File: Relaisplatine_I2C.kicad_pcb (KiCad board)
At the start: 2 copper layers, 85.1 x 114.9 mm, 74 parts, among them J1 K, J1.1 G1-K, J1.1a1001 G1-J, J1.1a1002 G1-K, J1.1a1003 G1-K, J1.1a1004 G1-K, J1.1a1005 G1-K, J1.1a1006 G1-K, J1.1a1007 G1-K, J1.2 G1-J, J1.2a1001 G1-K, J1.2a1002 G1-J, J1.2a1003 G1-J, J1.2a1004 G1-J, J1.2a1005 G1-J, J1.2a1006 G1-J, J1.2a1007 G1-J, J10 I²C, J11 Relais-Power, J12 Int, J2 J, J2.1 G2-K, J2.1a1001 G1-J, J2.2 G2-J, J2.2a1001 G2-K, J3.1 G3-K, J3.2 G3-J, J4.1 G4-K, J4.2 G4-J, J5.1 G5-K, J5.2 G5-J, J6.1 G6-K, J6.2 G6-J, J7.1 G7-K, J7.2 G7-J, J8.1 G8-K, J8.2 G8-J, U1 ULN2803A, U2 PCF8574

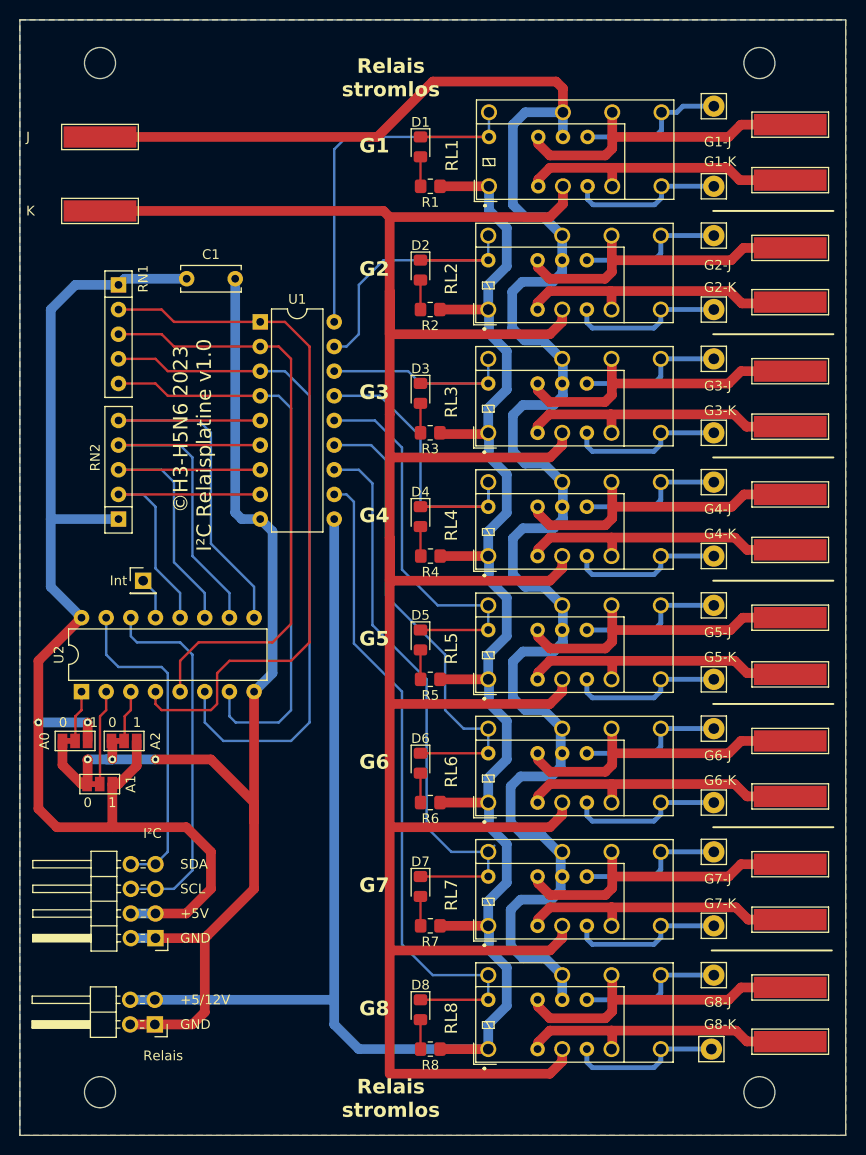
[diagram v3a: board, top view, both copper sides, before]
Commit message: Beschriftung für Gx-J|K vergrößert
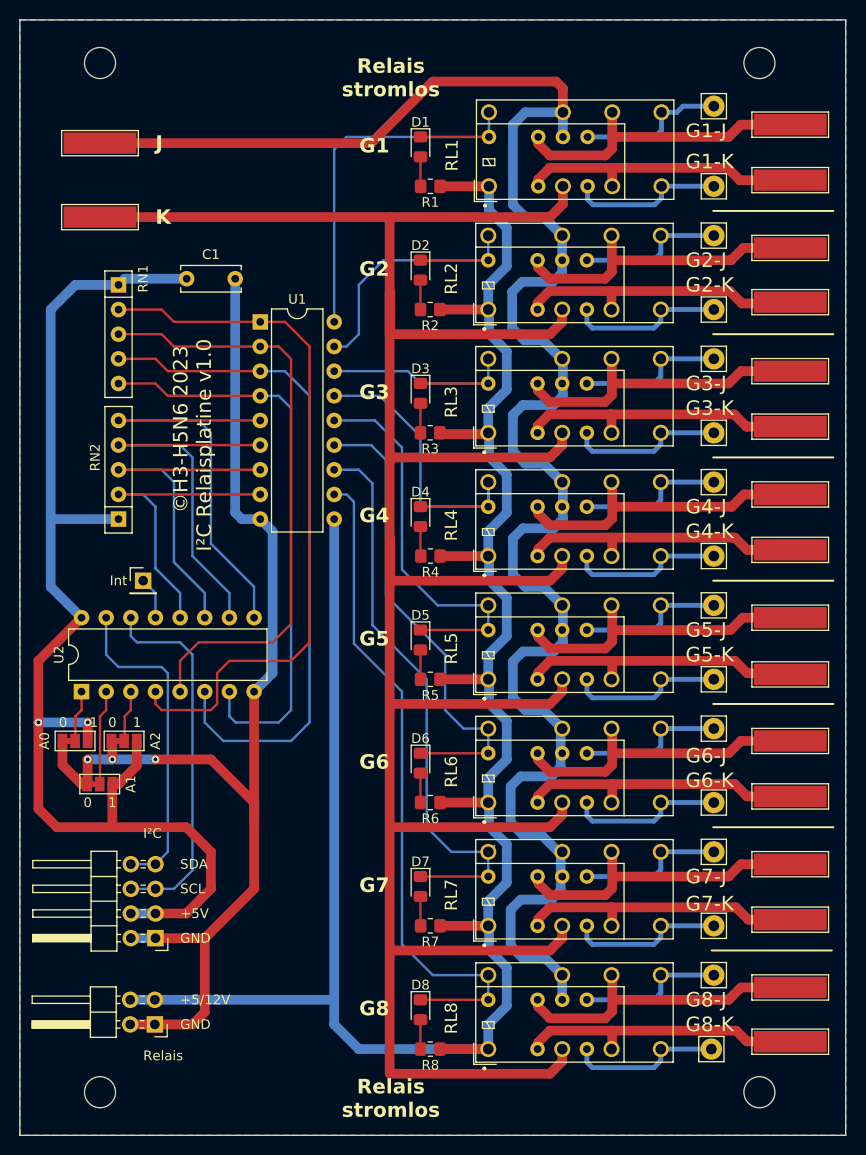
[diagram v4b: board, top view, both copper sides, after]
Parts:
- moved J1 0.64 mm to (67.3, 64.1)
- moved J2 0.63 mm to (67.3, 56.5)

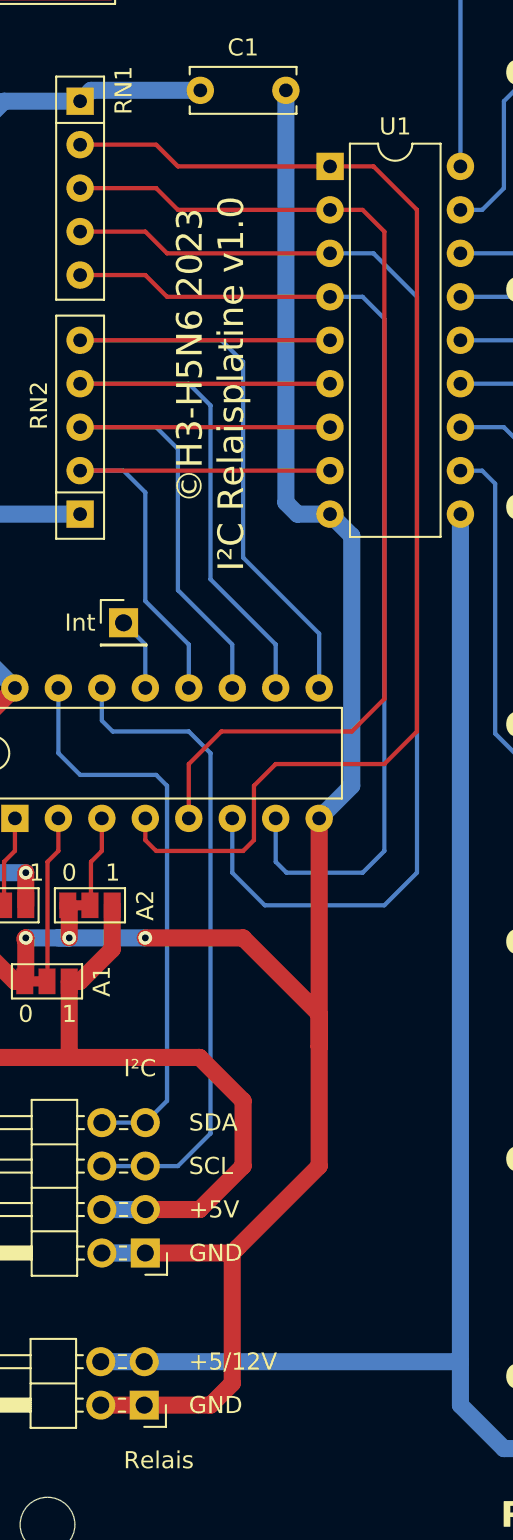
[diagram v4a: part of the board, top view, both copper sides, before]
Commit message: Power-LEDs für 5V und 12V hinzugefügt
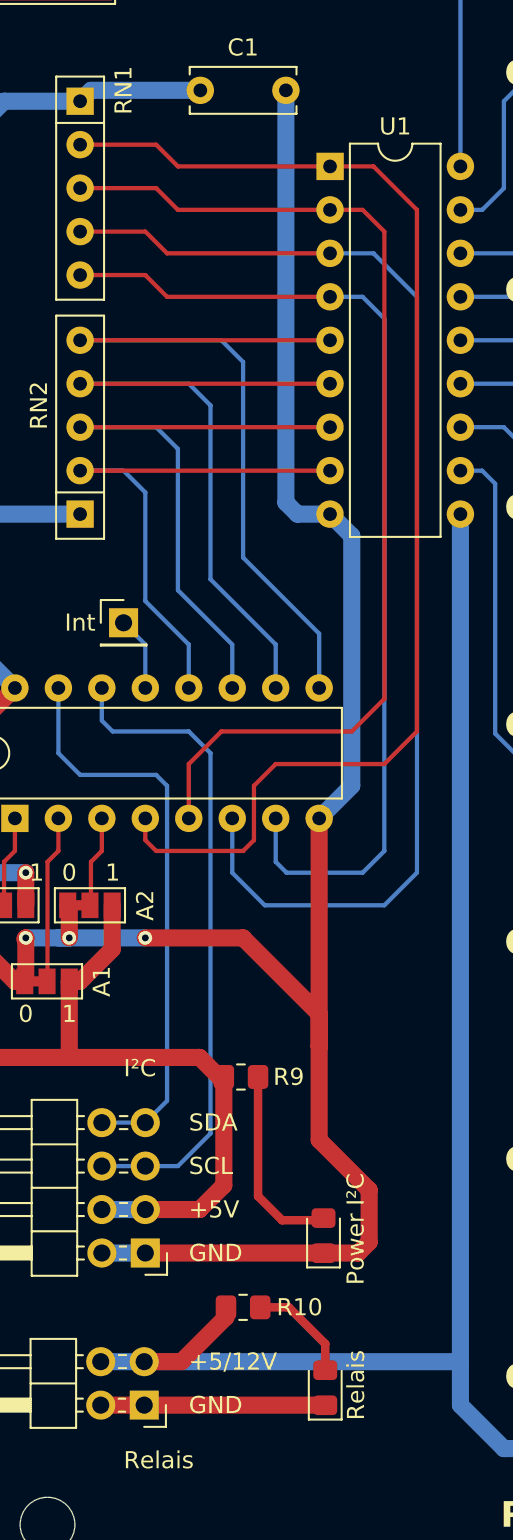
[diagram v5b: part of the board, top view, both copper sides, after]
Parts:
- added D10: Relais, LED_SMD:LED_0805_2012Metric_Pad1.15x1.40mm_HandSolder, F.Cu at (83.5, 146.3)
- added D9: Power I²C, LED_SMD:LED_0805_2012Metric_Pad1.15x1.40mm_HandSolder, F.Cu at (83.4, 137.4)
- added R10: 4k7, Resistor_SMD:R_0805_2012Metric_Pad1.20x1.40mm_HandSolder, F.Cu at (78.7, 141.6)
- added R9: 2k2, Resistor_SMD:R_0805_2012Metric_Pad1.20x1.40mm_HandSolder, F.Cu at (78.6, 128.1)
- RN1: value R_Network04 -> RN1
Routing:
- net Net-(D9-A): track 0.00 -> 11.4 mm
- net +12V: track 229.7 -> 236.1 mm
- net Net-(D10-A): track 0.00 -> 6.22 mm
- net GND: track 129.0 -> 133.0 mm
- net +5V: track 126.9 -> 126.2 mm
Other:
- board text removed: "©H3-H5N6 2023 I²C Relaisplatine v1.0"

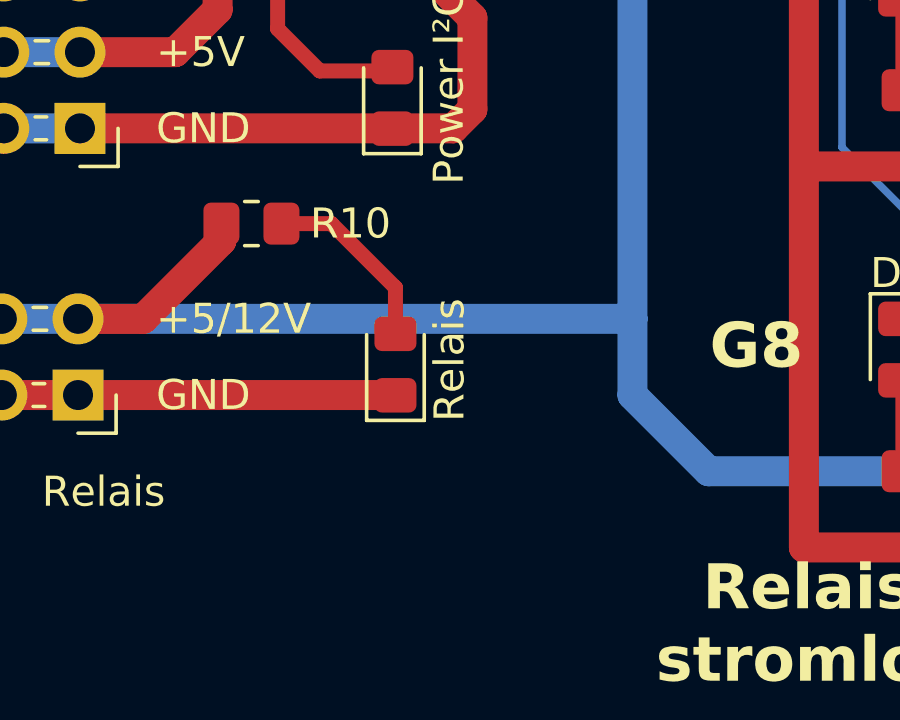
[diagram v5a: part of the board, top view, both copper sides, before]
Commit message: Revision als Feld, Widerstand der Ralais-LEDs auf 10k gesetzt
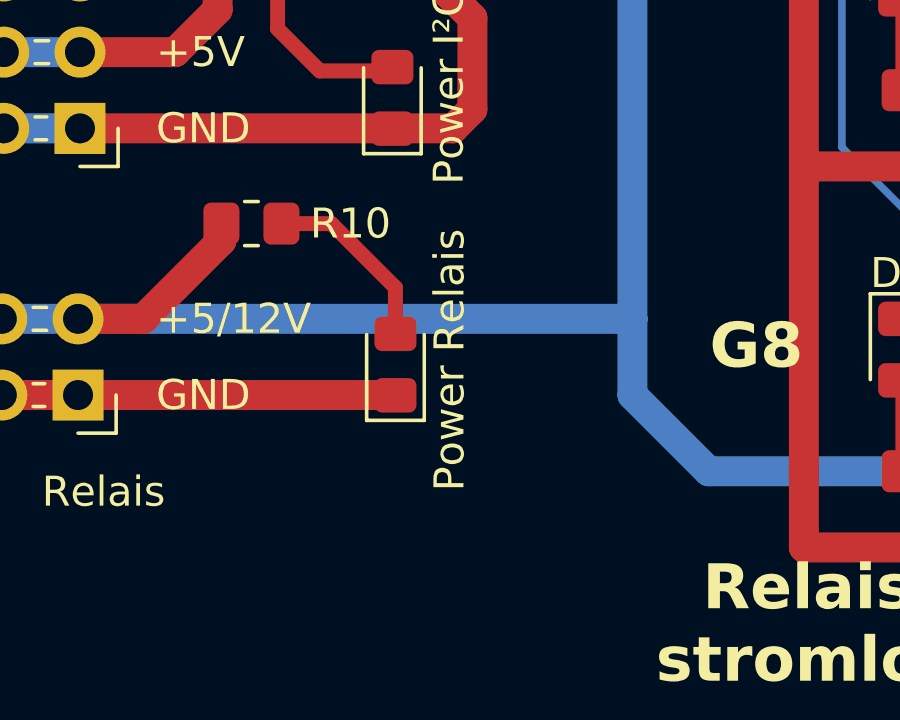
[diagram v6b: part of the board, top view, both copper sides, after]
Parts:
- D10: value Relais -> Power Relais
- R1, R2, R3, R4, R5, R6, R7, R8: value 1k -> 10k
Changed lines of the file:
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@@
     (descr "Resistor SMD 0805 (2012 Metric), square (rectangular) end terminal, IPC_7351 nominal with elongated pad for handsoldering. (Body size source: IPC-SM-782 page 72, https://www.pcb-3d.com/wordpress/wp-content/uploads/ipc-sm-782a_amendment_1_and_2.pdf), generated with kicad-footprint-generator")
     (tags "resistor handsolder")
+    (property "Quelle" "Resistor_SMD:R_0805_2012Metric_Pad1.20x1.40mm_HandSolder")
     (property "Sheetfile" "Relaisplatine_I2C.kicad_sch")
     (property "Sheetname" "")
@@
         (effects (font (size 1 1) (thickness 0.15)))
     )
-    (fp_text value "1k" (at 0 1.65) (layer "F.Fab")
+    (fp_text value "10k" (at 0 1.65) (layer "F.Fab")
         (effects (font (size 1 1) (thickness 0.15)))
     )
@@
     (descr "Resistor SMD 0805 (2012 Metric), square (rectangular) end terminal, IPC_7351 nominal with elongated pad for handsoldering. (Body size source: IPC-SM-782 page 72, https://www.pcb-3d.com/wordpress/wp-content/uploads/ipc-sm-782a_amendment_1_and_2.pdf), generated with kicad-footprint-generator")
     (tags "resistor handsolder")
+    (property "Quelle" "Resistor_SMD:R_0805_2012Metric_Pad1.20x1.40mm_HandSolder")
     (property "Sheetfile" "Relaisplatine_I2C.kicad_sch")
     (property "Sheetname" "")
@@
         (effects (font (size 1 1) (thickness 0.15)))
     )
-    (fp_text value "1k" (at 0 1.65) (layer "F.Fab")
+    (fp_text value "10k" (at 0 1.65) (layer "F.Fab")
         (effects (font (size 1 1) (thickness 0.15)))
     )
@@
     (descr "Resistor SMD 0805 (2012 Metric), square (rectangular) end terminal, IPC_7351 nominal with elongated pad for handsoldering. (Body size source: IPC-SM-782 page 72, https://www.pcb-3d.com/wordpress/wp-content/uploads/ipc-sm-782a_amendment_1_and_2.pdf), generated with kicad-footprint-generator")
     (tags "resistor handsolder")
+    (property "Quelle" "Resistor_SMD:R_0805_2012Metric_Pad1.20x1.40mm_HandSolder")
     (property "Sheetfile" "Relaisplatine_I2C.kicad_sch")
     (property "Sheetname" "")
@@
         (effects (font (size 1 1) (thickness 0.15)))
     )
-    (fp_text value "1k" (at 0 1.65 180) (layer "F.Fab")
+    (fp_text value "10k" (at 0 1.65 180) (layer "F.Fab")
         (effects (font (size 1 1) (thickness 0.15)))
     )
@@
     (descr "Resistor SMD 0805 (2012 Metric), square (rectangular) end terminal, IPC_7351 nominal with elongated pad for handsoldering. (Body size source: IPC-SM-782 page 72, https://www.pcb-3d.com/wordpress/wp-content/uploads/ipc-sm-782a_amendment_1_and_2.pdf), generated with kicad-footprint-generator")
     (tags "resistor handsolder")
+    (property "Quelle" "Resistor_SMD:R_0805_2012Metric_Pad1.20x1.40mm_HandSolder")
     (property "Sheetfile" "Relaisplatine_I2C.kicad_sch")
     (property "Sheetname" "")
@@
         (effects (font (size 1 1) (thickness 0.15)))
     )
-    (fp_text value "1k" (at 0 1.65 180) (layer "F.Fab")
+    (fp_text value "10k" (at 0 1.65 180) (layer "F.Fab")
         (effects (font (size 1 1) (thickness 0.15)))
     )
@@
     (descr "Resistor SMD 0805 (2012 Metric), square (rectangular) end terminal, IPC_7351 nominal with elongated pad for handsoldering. (Body size source: IPC-SM-782 page 72, https://www.pcb-3d.com/wordpress/wp-content/uploads/ipc-sm-782a_amendment_1_and_2.pdf), generated with kicad-footprint-generator")
     (tags "resistor handsolder")
+    (property "Quelle" "Resistor_SMD:R_0805_2012Metric_Pad1.20x1.40mm_HandSolder")
     (property "Sheetfile" "Relaisplatine_I2C.kicad_sch")
     (property "Sheetname" "")
@@
         (effects (font (size 1 1) (thickness 0.15)))
     )
-    (fp_text value "1k" (at 0 1.65) (layer "F.Fab")
+    (fp_text value "10k" (at 0 1.65) (layer "F.Fab")
         (effects (font (size 1 1) (thickness 0.15)))
     )
@@
     (descr "Resistor SMD 0805 (2012 Metric), square (rectangular) end terminal, IPC_7351 nominal with elongated pad for handsoldering. (Body size source: IPC-SM-782 page 72, https://www.pcb-3d.com/wordpress/wp-content/uploads/ipc-sm-782a_amendment_1_and_2.pdf), generated with kicad-footprint-generator")
     (tags "resistor handsolder")
+    (property "Quelle" "Resistor_SMD:R_0805_2012Metric_Pad1.20x1.40mm_HandSolder")
     (property "Sheetfile" "Relaisplatine_I2C.kicad_sch")
     (property "Sheetname" "")
@@
         (effects (font (size 1 1) (thickness 0.15)))
     )
-    (fp_text value "1k" (at 0 1.65) (layer "F.Fab")
+    (fp_text value "10k" (at 0 1.65) (layer "F.Fab")
         (effects (font (size 1 1) (thickness 0.15)))
     )
@@
     (descr "Resistor SMD 0805 (2012 Metric), square (rectangular) end terminal, IPC_7351 nominal with elongated pad for handsoldering. (Body size source: IPC-SM-782 page 72, https://www.pcb-3d.com/wordpress/wp-content/uploads/ipc-sm-782a_amendment_1_and_2.pdf), generated with kicad-footprint-generator")
     (tags "resistor handsolder")
+    (property "Quelle" "Resistor_SMD:R_0805_2012Metric_Pad1.20x1.40mm_HandSolder")
     (property "Sheetfile" "Relaisplatine_I2C.kicad_sch")
     (property "Sheetname" "")
@@
         (effects (font (size 1 1) (thickness 0.15)))
     )
-    (fp_text value "1k" (at 0 1.65) (layer "F.Fab")
+    (fp_text value "10k" (at 0 1.65) (layer "F.Fab")
         (effects (font (size 1 1) (thickness 0.15)))
     )
@@
     (descr "Resistor SMD 0805 (2012 Metric), square (rectangular) end terminal, IPC_7351 nominal with elongated pad for handsoldering. (Body size source: IPC-SM-782 page 72, https://www.pcb-3d.com/wordpress/wp-content/uploads/ipc-sm-782a_amendment_1_and_2.pdf), generated with kicad-footprint-generator")
     (tags "resistor handsolder")
+    (property "Quelle" "Resistor_SMD:R_0805_2012Metric_Pad1.20x1.40mm_HandSolder")
     (property "Sheetfile" "Relaisplatine_I2C.kicad_sch")
     (property "Sheetname" "")
@@
         (effects (font (size 1 1) (thickness 0.15)))
     )
-    (fp_text value "1k" (at 0 1.65) (layer "F.Fab")
+    (fp_text value "10k" (at 0 1.65) (layer "F.Fab")
         (effects (font (size 1 1) (thickness 0.15)))
     )
@@
         (effects (font (size 1 1) (thickness 0.15)))
     )
-    (fp_text value "Relais" (at 0.1524 1.8034 90) (layer "F.SilkS")
+    (fp_text value "Power Relais" (at 0.1524 1.8034 90) (layer "F.SilkS")
         (effects (font (size 1 1) (thickness 0.15)))
     )

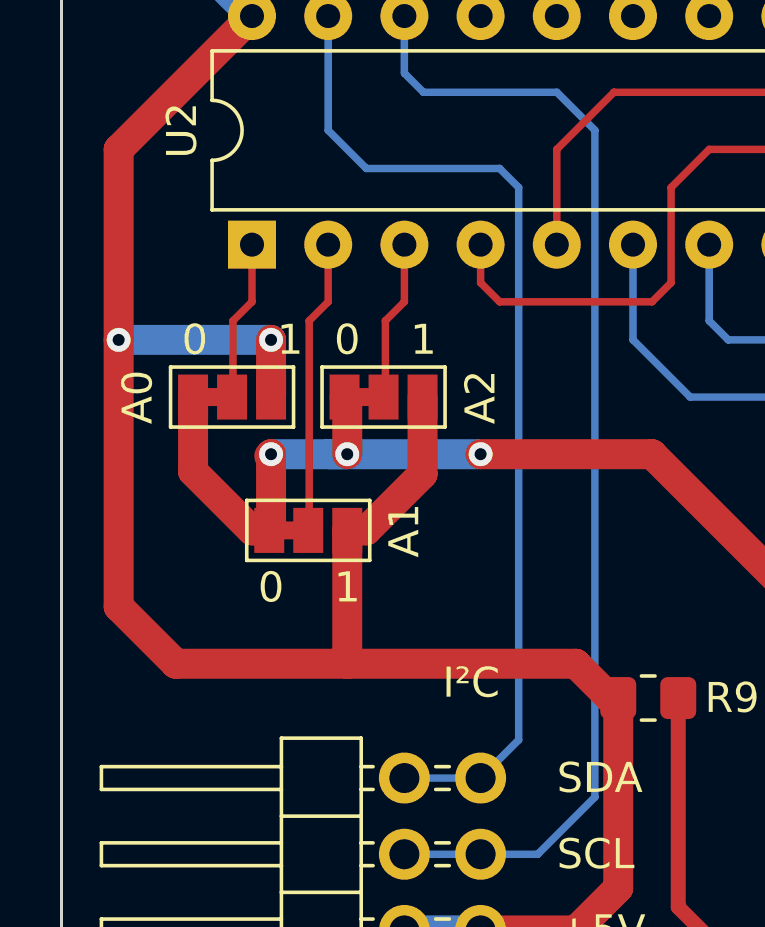
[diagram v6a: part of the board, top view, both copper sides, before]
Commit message: Abstand Fläche - Plarineneand auf 1mm gesetzt
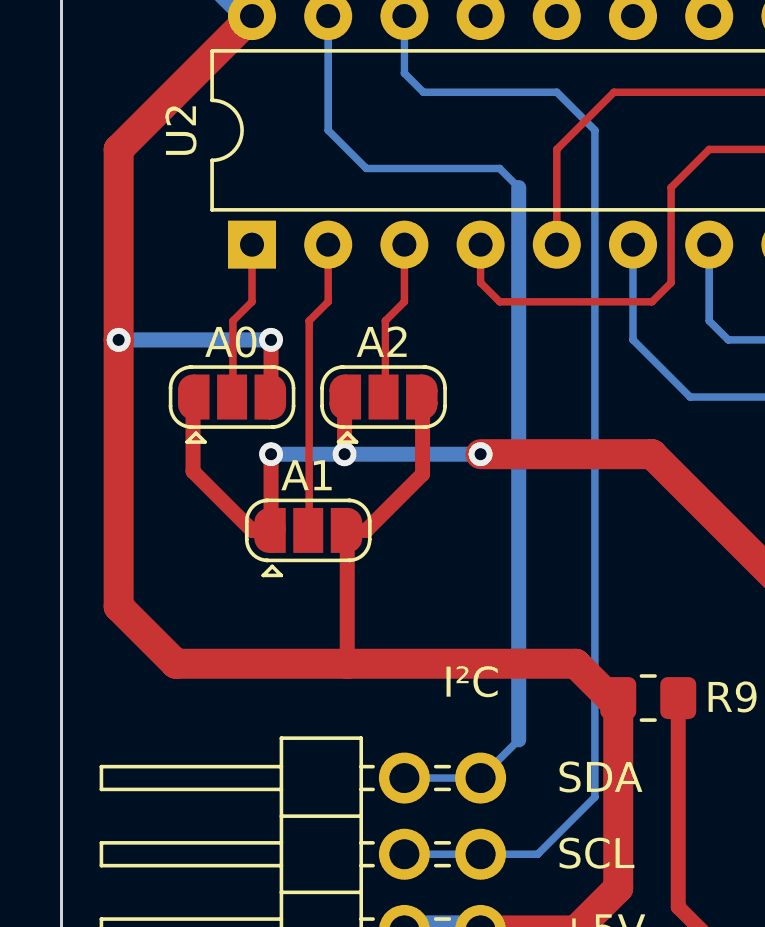
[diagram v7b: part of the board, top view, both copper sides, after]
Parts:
- A0, A1, A2: footprint Jumper:SolderJumper-3_P1.3mm_Bridged12_Pad1.0x1.5mm_NumberLabels -> Jumper:SolderJumper-3_P1.3mm_Open_RoundedPad1.0x1.5mm
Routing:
- net GND: track 133.0 -> 132.2 mm
